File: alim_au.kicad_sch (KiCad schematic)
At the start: 34 parts, among them U1 AMS1117-3.3

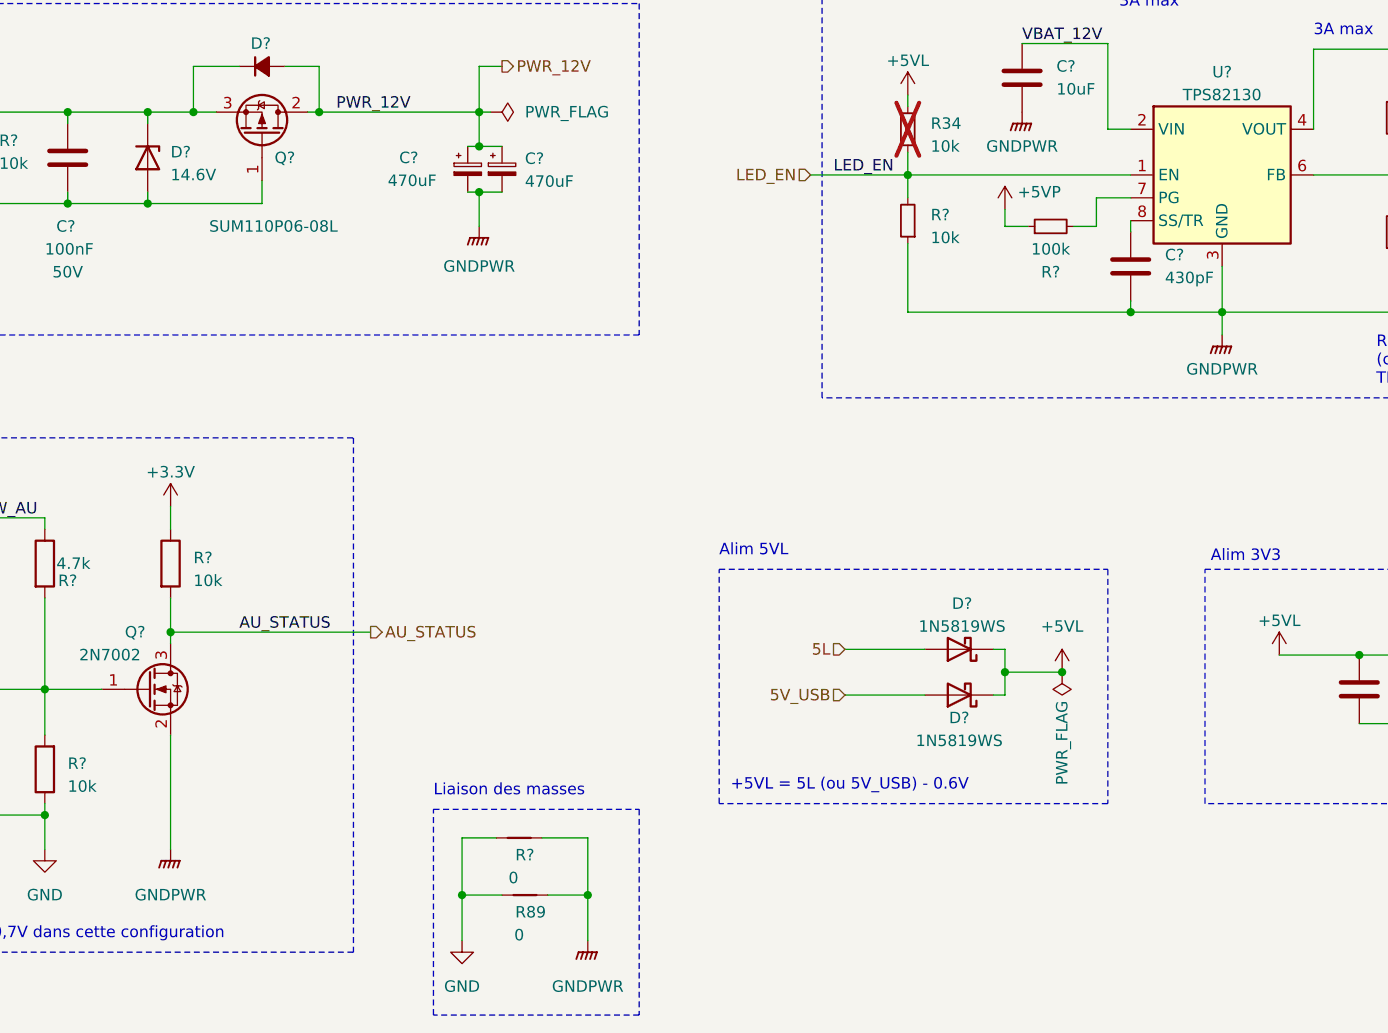
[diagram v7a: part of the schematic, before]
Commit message: nettoyage dossier et assignation de ref JLCPCB
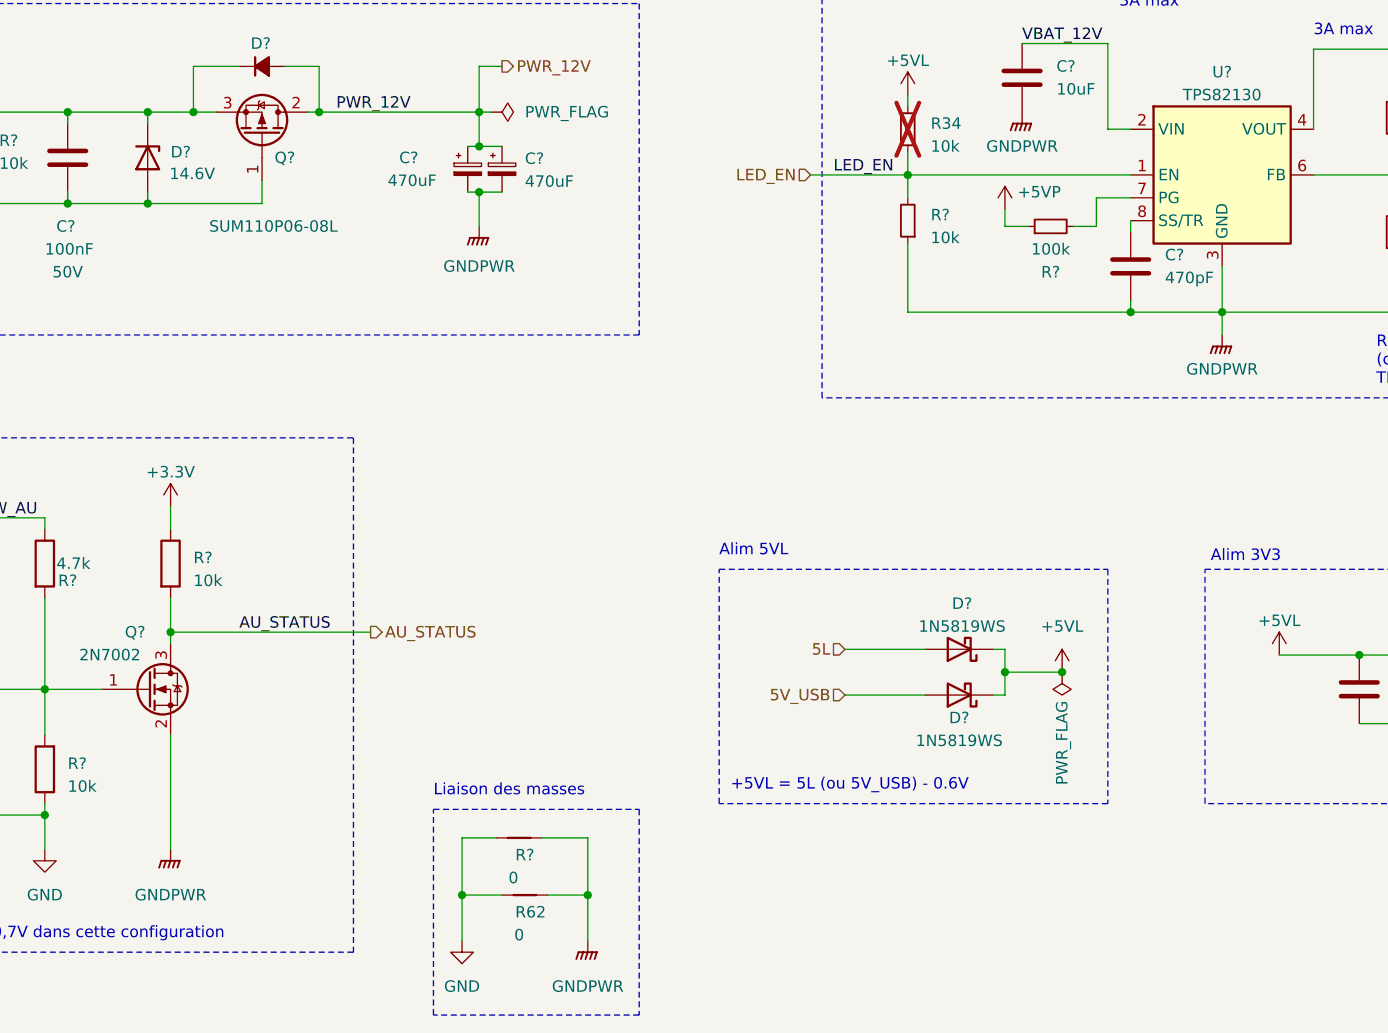
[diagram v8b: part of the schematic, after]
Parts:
- C?: footprint Capacitor_SMD:C_0603_1608Metric -> Capacitor_SMD:C_0805_2012Metric
- C?: value 430pF -> 470pF
- D?: value ~ -> RS3J R6
- D?: value 14.6V -> MM3Z15VST1G
- U1: footprint Package_TO_SOT_SMD:SOT-89-3 -> Package_TO_SOT_SMD:SOT-223-3_TabPin2
- renumbered R89 to R62
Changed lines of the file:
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@@
 			)
 		)
-		(property "Footprint" "Capacitor_SMD:C_0603_1608Metric"
+		(property "Footprint" "Capacitor_SMD:C_0805_2012Metric"
 			(at 251.7902 78.105 0)
 			(effects
@@
 			)
 		)
-		(property "Value" "~"
+		(property "Value" "RS3J R6"
 			(at 103.505 67.31 90)
 			(effects
@@
 			)
 		)
-		(property "Description" ""
+		(property "Description" "Switching 600V 3A"
 			(at 102.235 62.23 0)
 			(effects
@@
 			)
 		)
-		(property "Footprint" "Package_TO_SOT_SMD:SOT-89-3"
+		(property "Footprint" "Package_TO_SOT_SMD:SOT-223-3_TabPin2"
 			(at 238.125 122.555 0)
 			(effects
@@
 			)
 		)
-		(property "Description" ""
+		(property "Description" "860010474013"
 			(at 128.905 73.66 0)
 			(effects
@@
 		(on_board yes)
 		(dnp no)
-		(fields_autoplaced yes)
 		(property "Reference" "D?"
 			(at 92.075 71.755 90)
@@
 			)
 		)
-		(property "Value" "14.6V"
+		(property "Value" "MM3Z15VST1G"
 			(at 92.075 74.295 90)
 			(effects
@@
 				)
 				(justify left)
+				(hide yes)
 			)
 		)
 		(property "Footprint" "Diode_SMD:D_SOD-323_HandSoldering"
-			(at 89.535 72.39 0)
+			(at 82.804 72.644 0)
 			(effects
 				(font
@@
 			)
 		)
-		(property "Description" ""
-			(at 89.535 72.39 0)
+		(property "Description" "14.6V"
+			(at 94.488 74.168 90)
 			(effects
 				(font
 					(size 1.27 1.27)
 				)
-				(hide yes)
 			)
 		)
@@
 		(on_board yes)
 		(dnp no)
-		(property "Reference" "R89"
+		(property "Reference" "R62"
 			(at 132.08 156.21 0)
 			(effects
@@
 			(project "12v-actuators-pcb"
 				(path "/d0b6cc72-ff07-4f5e-a148-04b65c86a715/a9998e65-7bac-4337-98c8-7de7c845405f"
-					(reference "R89")
+					(reference "R62")
 					(unit 1)
 				)
@@
 			)
 		)
-		(property "Description" ""
+		(property "Description" "860010474013"
 			(at 125.095 73.66 0)
 			(effects
@@
 			)
 		)
-		(property "Value" "430pF"
+		(property "Value" "470pF"
 			(at 202.565 85.725 0)
 			(effects
